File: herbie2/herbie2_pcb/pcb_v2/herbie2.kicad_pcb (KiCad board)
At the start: 2 copper layers, 119.4 x 96.5 mm, 97 parts, among them J1 GND, J10 CONN_04JST-PTH, J11 CONN_04JST-PTH, J12 Vin, J15 Conn_01x03_Male, J16 Conn_02x03_Odd_Even, J17 Conn_01x03, J18 Conn_01x02, J19 Conn_01x01, J2 5V, J20 Conn_01x03, J3 I2C_STANDARDQWIIC, J4 Conn_01x01, J5 Conn_01x02, J8 I2C_STANDARDQWIIC, J9 I2C_STANDARDQWIIC, Q1 LTC4412, Q2 LTC4412, Q3 Si4427, Q4 Si4427, Q5 2N7002, U1 74HC595, U2 74164, U3 24v13_Pololu, U4 LS7366R, U5 LS7366R, U6 TCA9534, U7 24v13_Pololu, U8 D36V50F5_Pololu, Y1 20MHz, Y2 20MHz

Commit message: update v2 pcb
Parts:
- removed U1: 74HC595, Package_SO:SOIC-16_3.9x9.9mm_P1.27mm
- U6: footprint Package_SO:SOIC-16_4.55x10.3mm_P1.27mm -> Package_SO:SOIC-16W_7.5x10.3mm_P1.27mm
- moved Q1 12.0 mm to (165.1, 119.4), turned to 180 degrees
- moved Q2 12.0 mm to (153.7, 115.6), turned to 0 degrees
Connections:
- Q1 pad 1: BATT2 -> BATT1_F
- Q2 pad 1: BATT1_F -> BATT2
- Q3 pad 1: Net-(Q2-Pad5) -> Net-(Q1-Pad5)
- Q4 pad 1: Net-(Q1-Pad5) -> Net-(Q2-Pad5)
- R1 pad 1: Net-(Q1-Pad4) -> Net-(Q2-Pad4)
- R2 pad 1: Net-(Q2-Pad4) -> Net-(Q1-Pad4)
- S0 pad 1: Net-(S0-Pad1) -> DATA_SERVO
- S1 pad 1: Net-(S1-Pad1) -> RCLK_SERVO
- S2 pad 1: Net-(S2-Pad1) -> CLK_SERVO
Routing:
- net Net-(S0-Pad1): track 31.7 -> 0.00 mm, vias 2 -> 0
- net Net-(Q2-Pad5): track 38.5 -> 8.13 mm, vias 4 -> 0
- net Net-(Q1-Pad5): track 8.13 -> 38.5 mm, vias 0 -> 4
- net CLK_SERVO: track 42.1 -> 59.9 mm, vias 2 -> 0
- net Net-(S2-Pad1): track 17.1 -> 0.00 mm
- net Net-(S1-Pad1): track 16.1 -> 0.00 mm
- net DATA_SERVO: track 49.4 -> 65.3 mm, vias 4 -> 2
- net RCLK_SERVO: track 42.8 -> 58.6 mm, vias 2 -> 0
- net GND: track 197.8 -> 186.9 mm, vias 21 -> 20
- net Net-(R5-Pad1): track 18.7 -> 21.9 mm
- net 3.3V: track 401.4 -> 398.4 mm, vias 12 -> 11
- net LCD_BL: track 86.3 -> 88.7 mm
- net DI2: track 21.1 -> 19.4 mm
- net Net-(R3-Pad1): track 70.2 -> 68.8 mm
- net DI1: track 19.4 -> 18.0 mm
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
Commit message: updated v2 pcb
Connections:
- B2 pad A3: VIN_MEASURE -> SERVO3
- B2 pad A4: Net-(B2-PadA4) -> VIN_MEASURE
- J5 pad 2: Net-(B2-PadA4) -> VIN_MEASURE
- S3 pad 1: Net-(S3-Pad1) -> SERVO3
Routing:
- net SERVO3: track 0.00 -> 32.6 mm, vias 0 -> 4
- net Net-(S3-Pad1): track 21.5 -> 0.00 mm, vias 2 -> 0
- net Net-(S4-Pad1): track 22.6 -> 4.60 mm, vias 2 -> 0
- net Net-(S5-Pad1): track 23.3 -> 9.72 mm, vias 2 -> 0
- net GND: track 186.9 -> 178.0 mm
- net Net-(B2-PadA4): track 3.81 -> 0.00 mm
- net VIN_MEASURE: track 12.8 -> 13.7 mm, vias 2 -> 0
- net Net-(J11-Pad4): vias 1 -> 0
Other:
- board text added: "Herbie v0.2"
- board text removed: "Herbie v0.1"

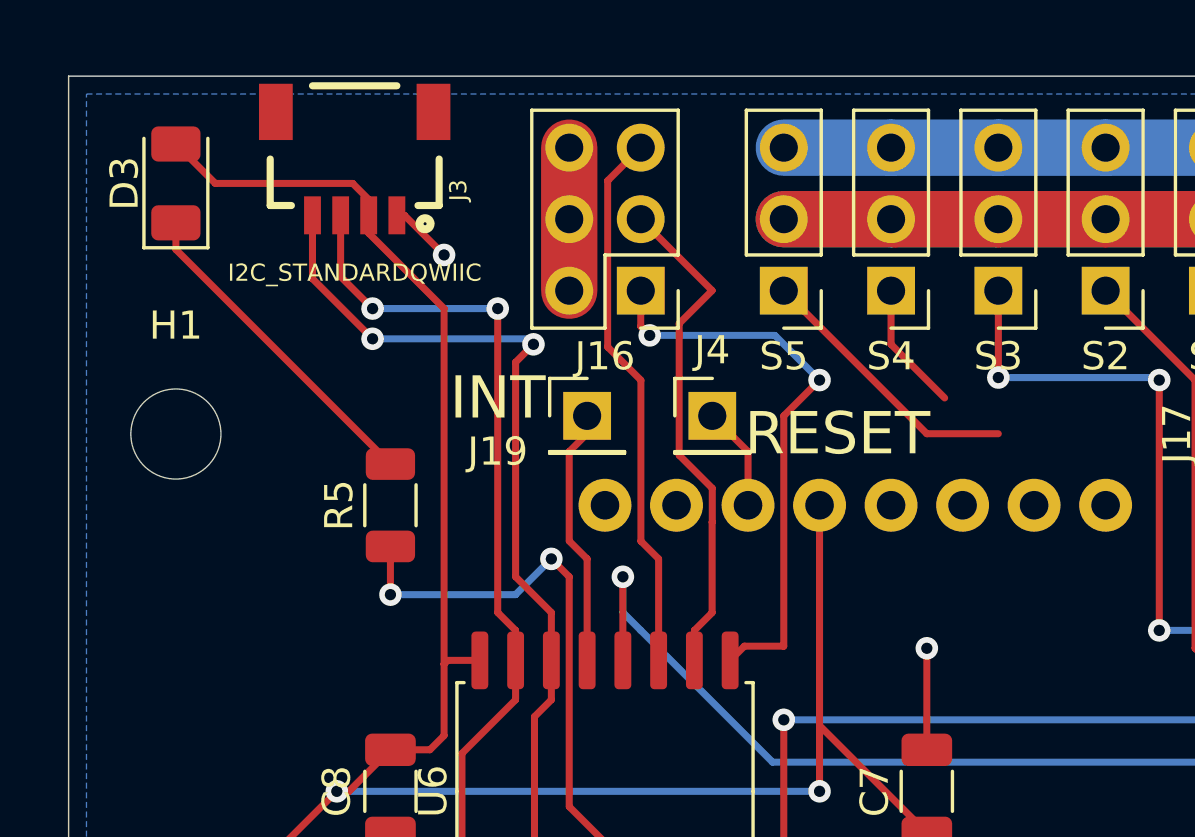
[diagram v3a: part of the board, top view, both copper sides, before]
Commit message: add switch
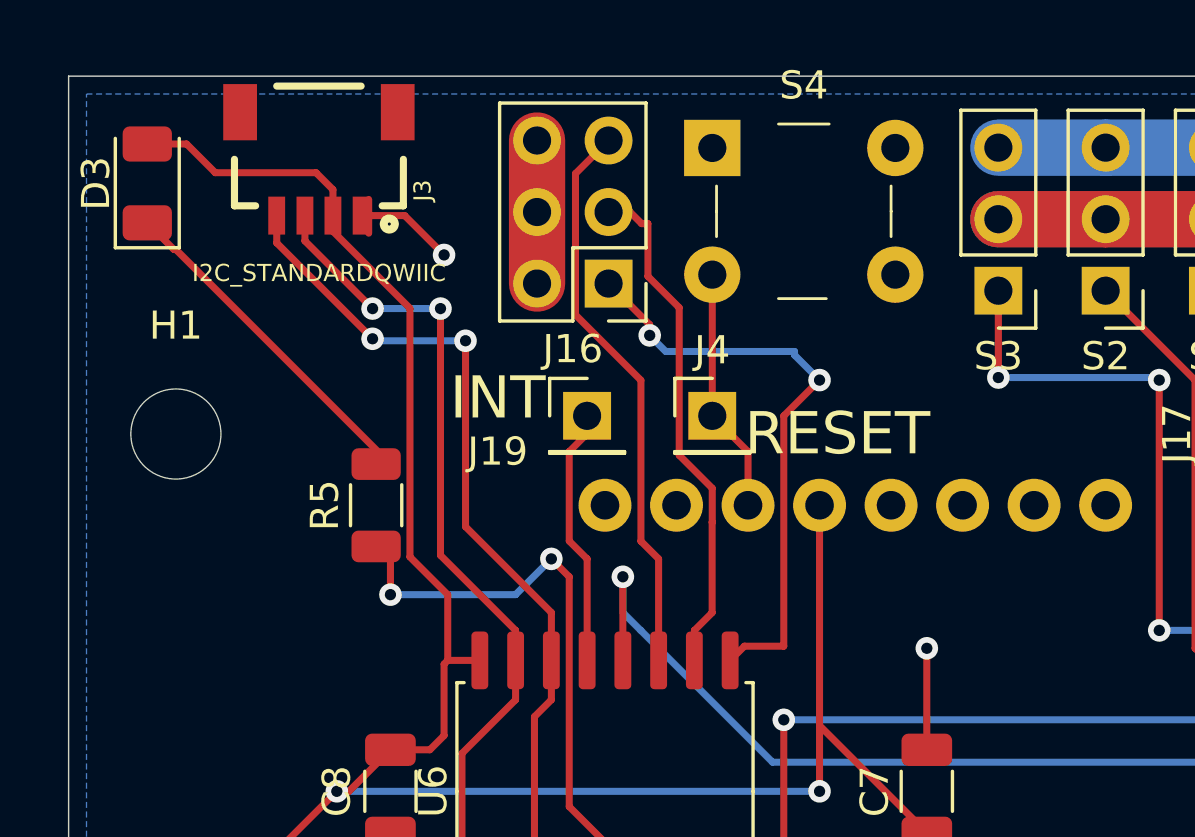
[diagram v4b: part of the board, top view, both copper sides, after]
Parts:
- removed S5: Servo5, Connector_PinHeader_2.54mm:PinHeader_1x03_P2.54mm_Vertical
- S4: value Servo4 -> B3F-1000; footprint Connector_PinHeader_2.54mm:PinHeader_1x03_P2.54mm_Vertical -> digikey-footprints:Switch_Tactile_THT_B3F-1xxx
- moved S4 8.13 mm to (125.7, 41.9), turned to 0 degrees
- moved J3 1.27 mm to (111.8, 44.3)
- moved J16 1.17 mm to (122.0, 46.7)
- moved D3 1.02 mm to (105.7, 43.2)
- moved R5 0.51 mm to (113.8, 54.6)
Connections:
- S4 pad 1: Net-(S4-Pad1) -> GND
- S4 pad 2: 5V_REG -> Net-(S4-Pad2)
- S4 pad 3: GND -> Net-(B2-PadRES)
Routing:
- net 5V_REG: track 181.8 -> 166.5 mm
- net Net-(S5-Pad1): track 9.72 -> 0.00 mm
- net GND: track 178.0 -> 172.9 mm
- net Net-(B2-PadRES): track 3.70 -> 8.72 mm
- net Net-(S4-Pad1): track 4.60 -> 0.00 mm
- net SCL: track 182.4 -> 181.1 mm
- net DI0: track 20.5 -> 21.3 mm
- net DI2: track 19.4 -> 20.2 mm
- net SDA: track 196.6 -> 195.9 mm

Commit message: updated pcb
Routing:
- net ENC2_SS: track 35.7 -> 41.1 mm
- net GND: track 172.9 -> 177.6 mm
- net 3.3V: track 398.8 -> 403.0 mm
- net E_STOP1: track 21.4 -> 25.6 mm
- net LCD_RS: track 36.6 -> 33.4 mm
- net ENC_SCK: track 95.0 -> 92.2 mm
- net Net-(LCD1-Pad15): track 19.4 -> 21.5 mm
- net SERVO3: track 32.6 -> 30.6 mm, vias 4 -> 2
- net Net-(R11-Pad2): track 29.5 -> 28.1 mm, vias 4 -> 2
- net Net-(J10-Pad3): track 29.3 -> 30.1 mm
- net 5V_REG: track 166.5 -> 167.1 mm
